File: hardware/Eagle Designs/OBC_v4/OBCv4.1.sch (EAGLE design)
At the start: 32 parts, among them J1 5037630291, J16 U.FL-R-SMT-1(01), J2 5037630491, J3 5037630591, J4 5037630291, J5 5037630491, J6 5037630291, J7 503763-0691, J8 503763-0691, J9 U.FL-R-SMT-1(01)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

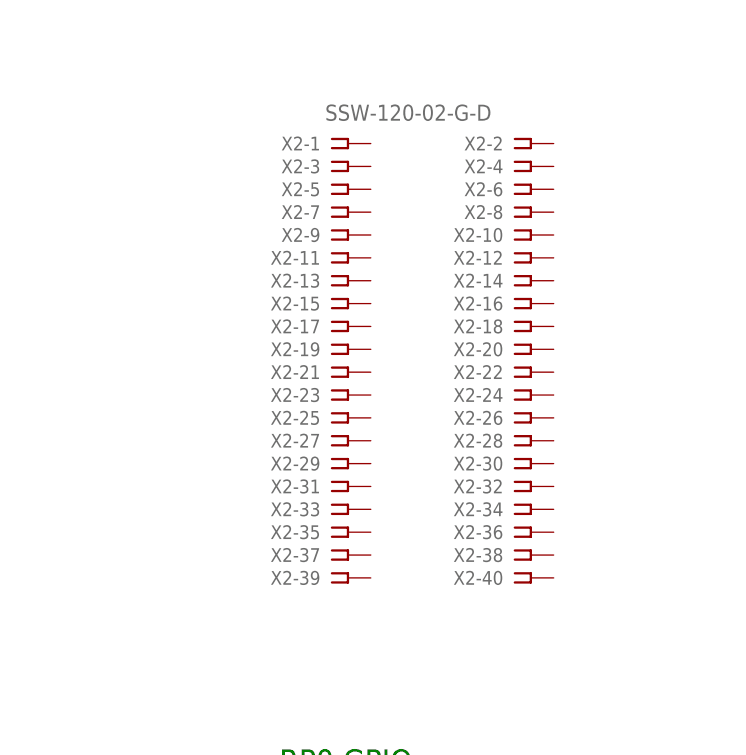
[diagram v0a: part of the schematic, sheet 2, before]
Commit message: Finalized PDU Battery Charging Circuit Design And Added Gerber Files
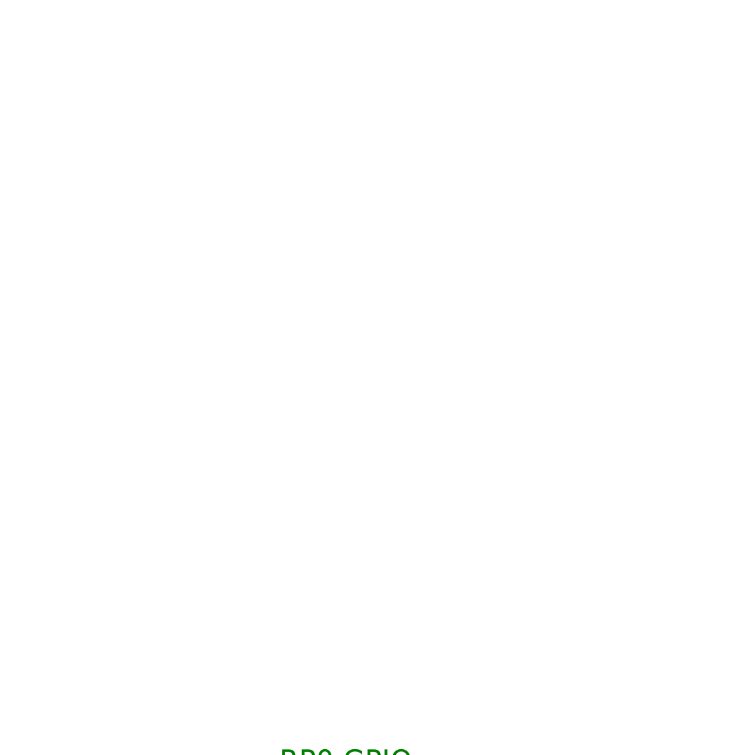
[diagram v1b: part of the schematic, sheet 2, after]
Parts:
- removed X2: SSW-120-02-G-D, con-samtec-edited:SSW-120-02-G-D
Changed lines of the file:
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@@
 <part name="L1" library="L" deviceset="L" device=""/>
 <part name="R6" library="HSFL_Main_Library" deviceset="RESISTOR" device="0805-RES" value="0"/>
-<part name="X2" library="con-samtec-edited" deviceset="SSW-120-02-G" device="-D"/>
 <part name="U$1" library="OBCv4" deviceset="TEENSY41" device=""/>
 <part name="J1" library="OBCv4" deviceset="5037630291" device="" package3d_urn="urn:adsk.eagle:package:30936816/1"/>
@@
 <attribute name="VALUE" x="-88.9" y="30.48" size="1.778" layer="96"/>
 </instance>
-<instance part="X2" gate="-1" x="5.08" y="162.56" smashed="yes">
-<attribute name="VALUE" x="2.54" y="165.1" size="1.778" layer="96"/>
-<attribute name="NAME" x="2.032" y="163.322" size="1.524" layer="95" rot="R180"/>
-</instance>
-<instance part="X2" gate="-2" x="25.4" y="162.56" smashed="yes">
-<attribute name="NAME" x="22.352" y="163.322" size="1.524" layer="95" rot="R180"/>
-</instance>
-<instance part="X2" gate="-3" x="5.08" y="160.02" smashed="yes">
-<attribute name="NAME" x="2.032" y="160.782" size="1.524" layer="95" rot="R180"/>
-</instance>
-<instance part="X2" gate="-4" x="25.4" y="160.02" smashed="yes">
-<attribute name="NAME" x="22.352" y="160.782" size="1.524" layer="95" rot="R180"/>
-</instance>
-<instance part="X2" gate="-5" x="5.08" y="157.48" smashed="yes">
-<attribute name="NAME" x="2.032" y="158.242" size="1.524" layer="95" rot="R180"/>
-</instance>
-<instance part="X2" gate="-6" x="25.4" y="157.48" smashed="yes">
-<attribute name="NAME" x="22.352" y="158.242" size="1.524" layer="95" rot="R180"/>
-</instance>
-<instance part="X2" gate="-7" x="5.08" y="154.94" smashed="yes">
-<attribute name="NAME" x="2.032" y="155.702" size="1.524" layer="95" rot="R180"/>
-</instance>
-<instance part="X2" gate="-8" x="25.4" y="154.94" smashed="yes">
-<attribute name="NAME" x="22.352" y="155.702" size="1.524" layer="95" rot="R180"/>
-</instance>
-<instance part="X2" gate="-9" x="5.08" y="152.4" smashed="yes">
-<attribute name="NAME" x="2.032" y="153.162" size="1.524" layer="95" rot="R180"/>
-</instance>
-<instance part="X2" gate="-10" x="25.4" y="152.4" smashed="yes">
-<attribute name="NAME" x="22.352" y="153.162" size="1.524" layer="95" rot="R180"/>
-</instance>
-<instance part="X2" gate="-11" x="5.08" y="149.86" smashed="yes">
-<attribute name="NAME" x="2.032" y="150.622" size="1.524" layer="95" rot="R180"/>
-</instance>
-<instance part="X2" gate="-12" x="25.4" y="149.86" smashed="yes">
-<attribute name="NAME" x="22.352" y="150.622" size="1.524" layer="95" rot="R180"/>
-</instance>
-<instance part="X2" gate="-13" x="5.08" y="147.32" smashed="yes">
-<attribute name="NAME" x="2.032" y="148.082" size="1.524" layer="95" rot="R180"/>
-</instance>
-<instance part="X2" gate="-14" x="25.4" y="147.32" smashed="yes">
-<attribute name="NAME" x="22.352" y="148.082" size="1.524" layer="95" rot="R180"/>
-</instance>
-<instance part="X2" gate="-15" x="5.08" y="144.78" smashed="yes">
-<attribute name="NAME" x="2.032" y="145.542" size="1.524" layer="95" rot="R180"/>
-</instance>
-<instance part="X2" gate="-16" x="25.4" y="144.78" smashed="yes">
-<attribute name="NAME" x="22.352" y="145.542" size="1.524" layer="95" rot="R180"/>
-</instance>
-<instance part="X2" gate="-17" x="5.08" y="142.24" smashed="yes">
-<attribute name="NAME" x="2.032" y="143.002" size="1.524" layer="95" rot="R180"/>
-</instance>
-<instance part="X2" gate="-18" x="25.4" y="142.24" smashed="yes">
-<attribute name="NAME" x="22.352" y="143.002" size="1.524" layer="95" rot="R180"/>
-</instance>
-<instance part="X2" gate="-19" x="5.08" y="139.7" smashed="yes">
-<attribute name="NAME" x="2.032" y="140.462" size="1.524" layer="95" rot="R180"/>
-</instance>
-<instance part="X2" gate="-20" x="25.4" y="139.7" smashed="yes">
-<attribute name="NAME" x="22.352" y="140.462" size="1.524" layer="95" rot="R180"/>
-</instance>
-<instance part="X2" gate="-21" x="5.08" y="137.16" smashed="yes">
-<attribute name="NAME" x="2.032" y="137.922" size="1.524" layer="95" rot="R180"/>
-</instance>
-<instance part="X2" gate="-22" x="25.4" y="137.16" smashed="yes">
-<attribute name="NAME" x="22.352" y="137.922" size="1.524" layer="95" rot="R180"/>
-</instance>
-<instance part="X2" gate="-23" x="5.08" y="134.62" smashed="yes">
-<attribute name="NAME" x="2.032" y="135.382" size="1.524" layer="95" rot="R180"/>
-</instance>
-<instance part="X2" gate="-24" x="25.4" y="134.62" smashed="yes">
-<attribute name="NAME" x="22.352" y="135.382" size="1.524" layer="95" rot="R180"/>
-</instance>
-<instance part="X2" gate="-25" x="5.08" y="132.08" smashed="yes">
-<attribute name="NAME" x="2.032" y="132.842" size="1.524" layer="95" rot="R180"/>
-</instance>
-<instance part="X2" gate="-26" x="25.4" y="132.08" smashed="yes">
-<attribute name="NAME" x="22.352" y="132.842" size="1.524" layer="95" rot="R180"/>
-</instance>
-<instance part="X2" gate="-27" x="5.08" y="129.54" smashed="yes">
-<attribute name="NAME" x="2.032" y="130.302" size="1.524" layer="95" rot="R180"/>
-</instance>
-<instance part="X2" gate="-28" x="25.4" y="129.54" smashed="yes">
-<attribute name="NAME" x="22.352" y="130.302" size="1.524" layer="95" rot="R180"/>
-</instance>
-<instance part="X2" gate="-29" x="5.08" y="127" smashed="yes">
-<attribute name="NAME" x="2.032" y="127.762" size="1.524" layer="95" rot="R180"/>
-</instance>
-<instance part="X2" gate="-30" x="25.4" y="127" smashed="yes">
-<attribute name="NAME" x="22.352" y="127.762" size="1.524" layer="95" rot="R180"/>
-</instance>
-<instance part="X2" gate="-31" x="5.08" y="124.46" smashed="yes">
-<attribute name="NAME" x="2.032" y="125.222" size="1.524" layer="95" rot="R180"/>
-</instance>
-<instance part="X2" gate="-32" x="25.4" y="124.46" smashed="yes">
-<attribute name="NAME" x="22.352" y="125.222" size="1.524" layer="95" rot="R180"/>
-</instance>
-<instance part="X2" gate="-33" x="5.08" y="121.92" smashed="yes">
-<attribute name="NAME" x="2.032" y="122.682" size="1.524" layer="95" rot="R180"/>
-</instance>
-<instance part="X2" gate="-34" x="25.4" y="121.92" smashed="yes">
-<attribute name="NAME" x="22.352" y="122.682" size="1.524" layer="95" rot="R180"/>
-</instance>
-<instance part="X2" gate="-35" x="5.08" y="119.38" smashed="yes">
-<attribute name="NAME" x="2.032" y="120.142" size="1.524" layer="95" rot="R180"/>
-</instance>
-<instance part="X2" gate="-36" x="25.4" y="119.38" smashed="yes">
-<attribute name="NAME" x="22.352" y="120.142" size="1.524" layer="95" rot="R180"/>
-</instance>
-<instance part="X2" gate="-37" x="5.08" y="116.84" smashed="yes">
-<attribute name="NAME" x="2.032" y="117.602" size="1.524" layer="95" rot="R180"/>
-</instance>
-<instance part="X2" gate="-38" x="25.4" y="116.84" smashed="yes">
-<attribute name="NAME" x="22.352" y="117.602" size="1.524" layer="95" rot="R180"/>
-</instance>
-<instance part="X2" gate="-39" x="5.08" y="114.3" smashed="yes">
-<attribute name="NAME" x="2.032" y="115.062" size="1.524" layer="95" rot="R180"/>
-</instance>
-<instance part="X2" gate="-40" x="25.4" y="114.3" smashed="yes">
-<attribute name="NAME" x="22.352" y="115.062" size="1.524" layer="95" rot="R180"/>
-</instance>
 <instance part="J6" gate="A" x="2.54" y="33.02" smashed="yes">
